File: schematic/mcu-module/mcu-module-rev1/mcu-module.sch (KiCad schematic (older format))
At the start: 21 parts

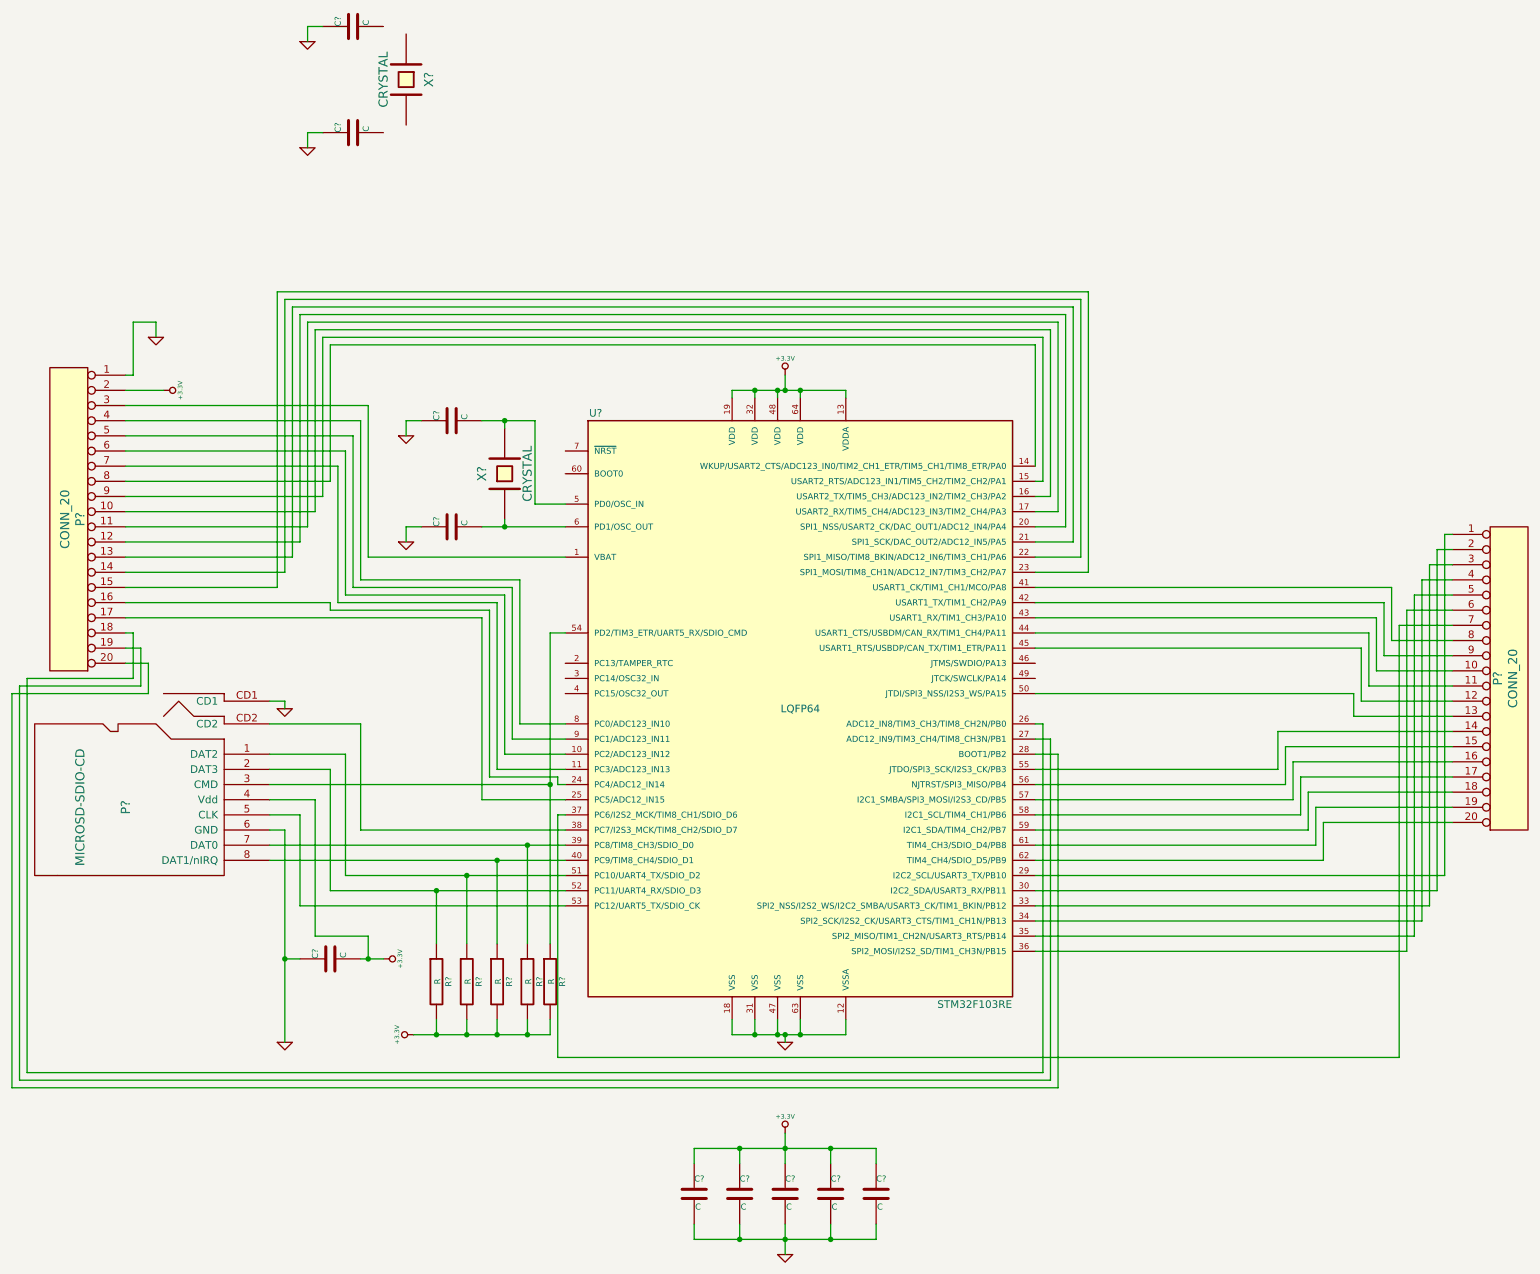
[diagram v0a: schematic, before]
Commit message: MCU module pcb created and close to be done
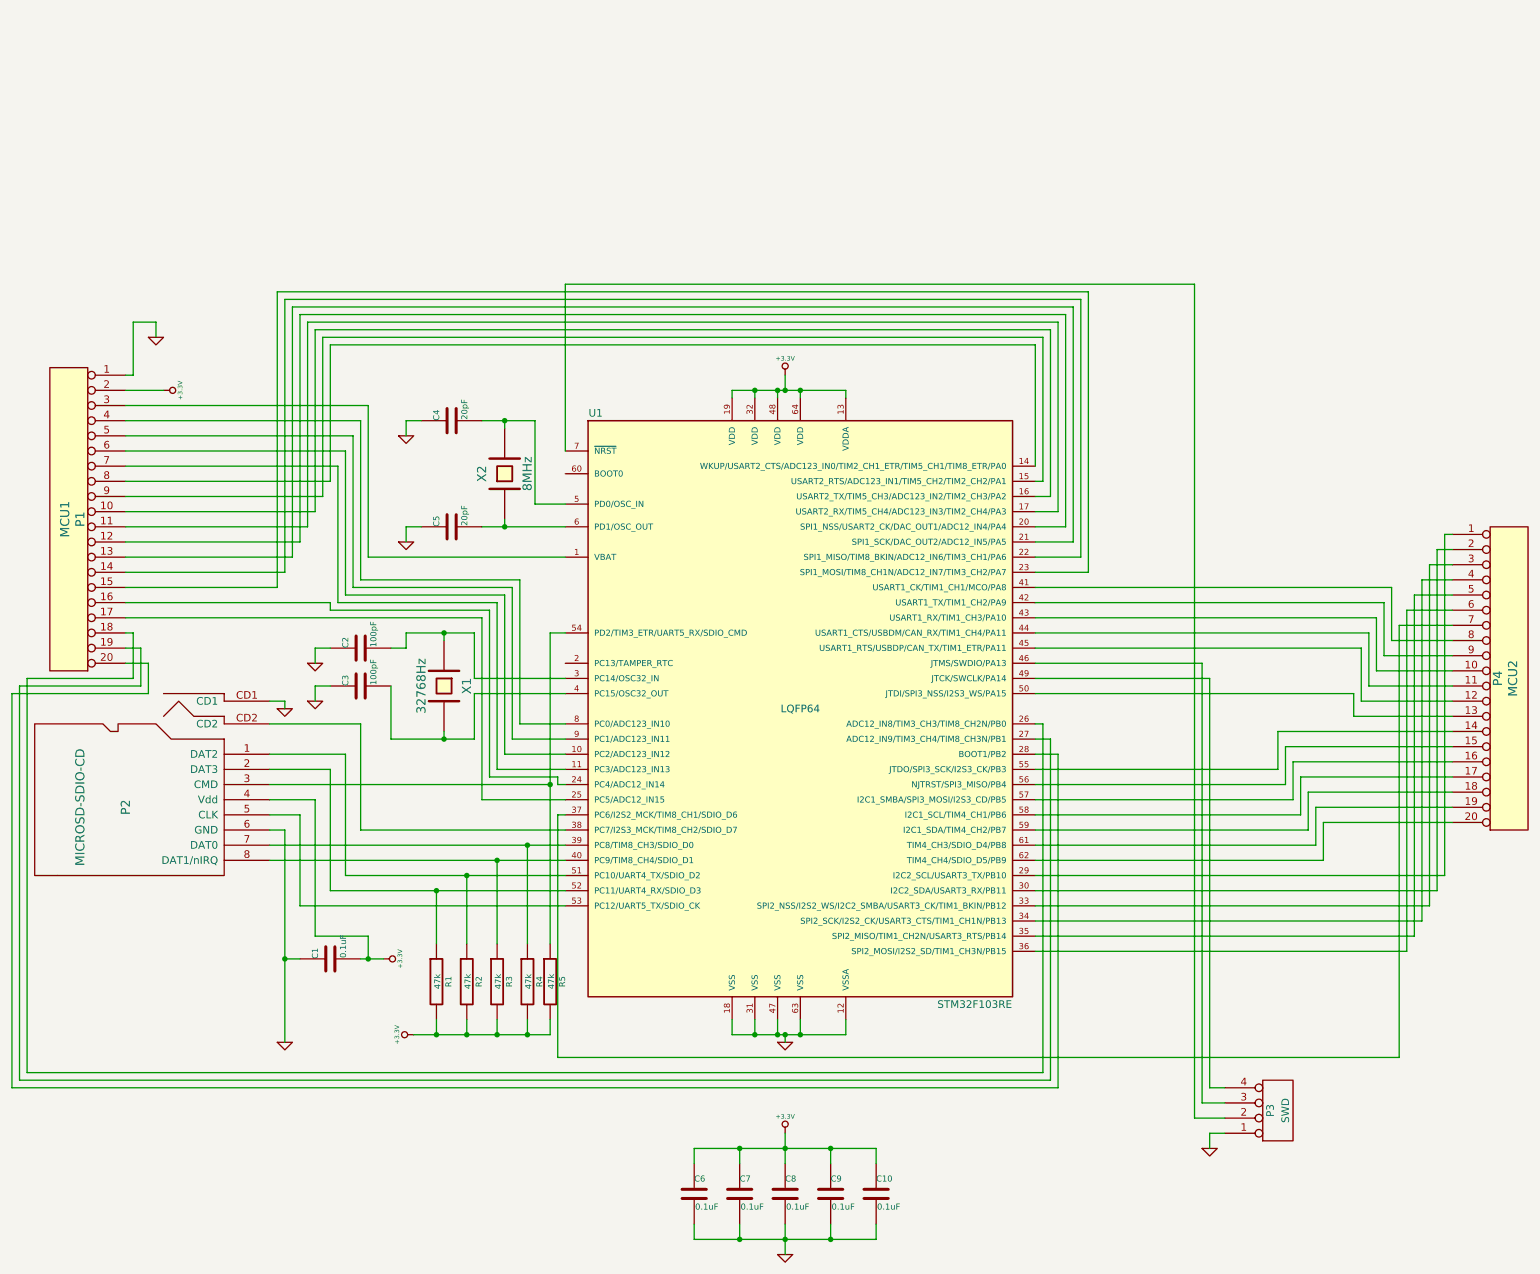
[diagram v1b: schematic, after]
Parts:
- added P3: SWD, ~, symbol CONN_4
- C1, C10, C6, C7, C8, C9: renamed from C?; value C -> 0.1uF
- C2, C3: renamed from C?; value C -> 100pF
- C4, C5: renamed from C?; value C -> 20pF
- P1: renamed from P?; value CONN_20 -> MCU1
- P4: renamed from P?; value CONN_20 -> MCU2
- R1, R2, R3, R4, R5: renamed from R?; value R -> 47k
- X1: renamed from X?; value CRYSTAL -> 32768Hz
- X2: renamed from X?; value CRYSTAL -> 8MHz
- gave numbers to parts that had none: 2
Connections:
- net GND: now also P3.1 (P1)
- net at U1.3 (PC14/OSC32_IN): now also C2.2, X1.1
- net at U1.4 (PC15/OSC32_OUT): now also C3.2, X1.2
- net at U1.46 (JTMS/SWDIO/PA13): now also P3.3 (P3)
- net at U1.49 (JTCK/SWCLK/PA14): now also P3.4 (P4)
- net at U1.7 (~NRST): now also P3.2 (P2)
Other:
- moved on the sheet: C2, C3, X1
